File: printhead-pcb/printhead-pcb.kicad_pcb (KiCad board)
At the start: 2 copper layers, 35 x 35 mm, 30 parts, among them J1 Power, J13 Steckverbinder_Male_1, J3 DATA, U1 PCA9615DP, U6 AP7361C-33E

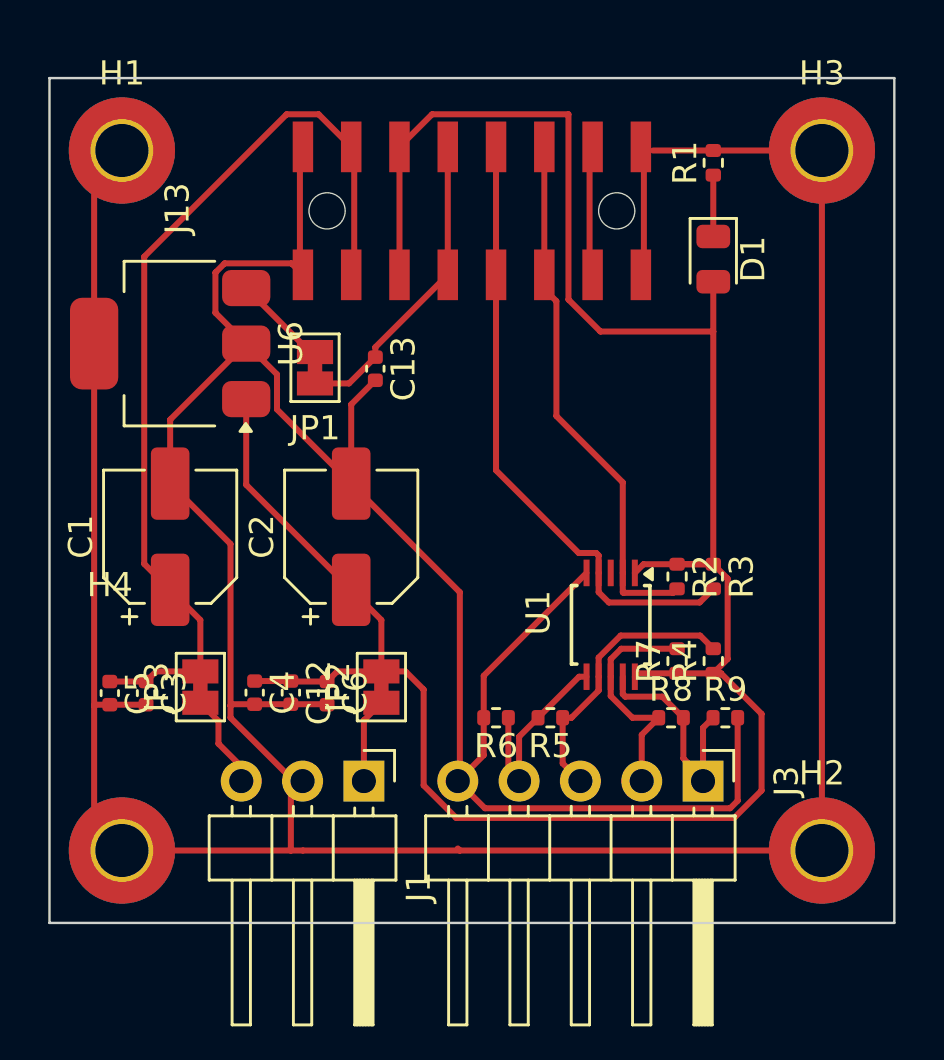
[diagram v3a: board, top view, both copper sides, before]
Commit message: working, good version with one layer and equally long signal routes, thicker traces and fitting text
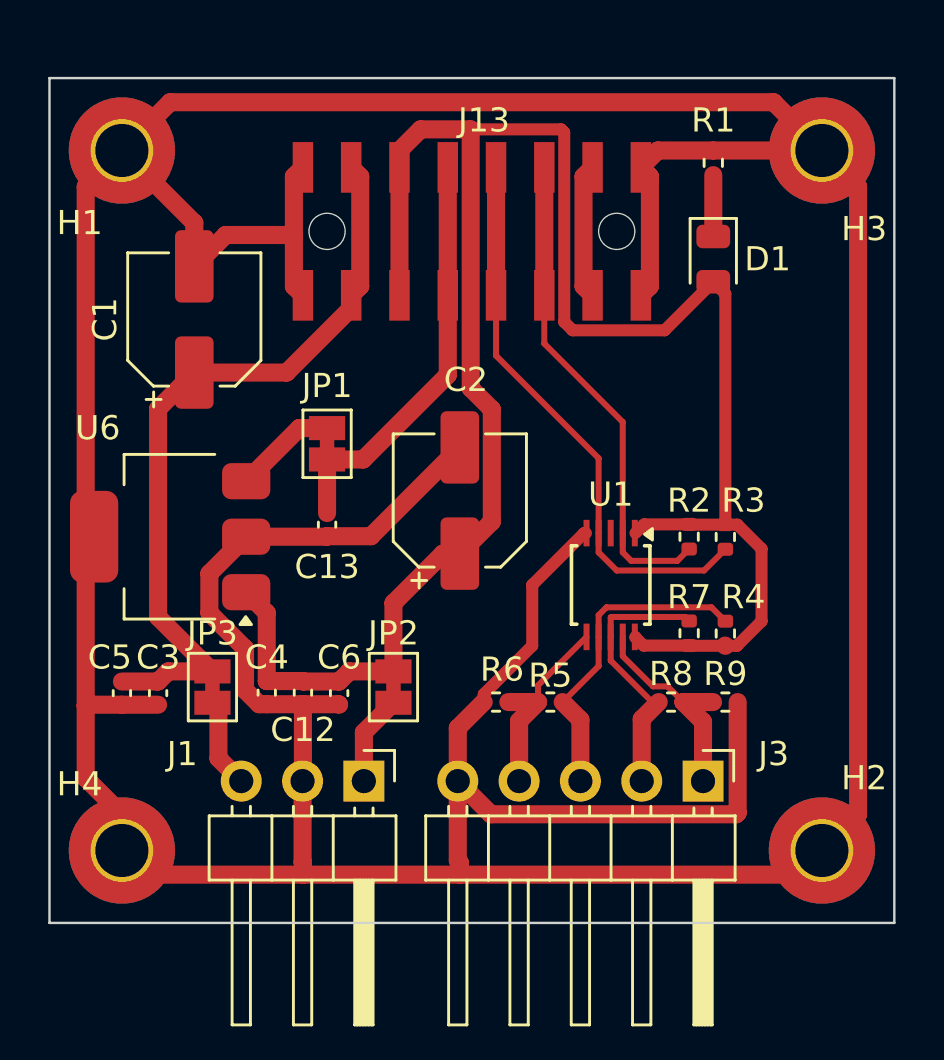
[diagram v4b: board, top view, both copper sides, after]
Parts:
- moved C1 9.06 mm to (106.0, 110.0)
- moved U6 8.00 mm to (105.0, 119.0)
- moved C13 6.76 mm to (111.5, 118.5)
- moved C2 4.74 mm to (117.0, 117.5)
- moved JP1 3.19 mm to (111.5, 115.2)
- moved R2 1.72 mm to (126.5, 119.0)
- moved R3 1.71 mm to (128.0, 119.0)
- moved U1 1.65 mm to (123.2, 121.0)
- moved R7 1.25 mm to (126.5, 123.0)
- moved R4 1.24 mm to (128.0, 123.0)
- moved J13 0.85 mm to (110.5, 109.0)
- moved R5 0.65 mm to (120.8, 125.8)
- moved R6 0.65 mm to (118.5, 125.8)
- moved R8 0.65 mm to (125.8, 125.8)
- moved R9 0.65 mm to (128.0, 125.8)
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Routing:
- net GND: track 197.8 -> 216.8 mm
- net +5V: track 98.3 -> 87.5 mm
- net +12V: track 39.0 -> 31.6 mm
- net +3V3: track 12.9 -> 17.3 mm
- net SCL: track 25.8 -> 23.6 mm
- net DSCLP: track 11.6 -> 13.4 mm
- net SDA: track 22.1 -> 20.4 mm
- net DSDAP: track 9.73 -> 11.4 mm
